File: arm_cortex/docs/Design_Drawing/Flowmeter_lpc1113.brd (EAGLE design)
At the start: 160 x 100 mm, 99 parts, among them IC1 LM7805, IC2 LM324N, IC5 OP07CN, Q4 BSS92, Q5 BSS295, U1 LPC1113FBD48/302,1, U2 LD1117S33CTR, U4 MAX232ACSE+, U5 MAX485CSA+, X1 MKDSN1,5/3-5,08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

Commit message: removed 4-20mA translation circuit. removed the power 10V supply. added +12V and -12V supply regulator. added bridge rectifier
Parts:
- removed C11, C12: 100n, rcl:C0805K
- removed D1, D2: (no value), diode:MINIMELF
- removed D10, D9: 1N4004, diode:DO41-10
- removed D3: (no value), fabisp:NG_SOD123
- removed JP3: (no value), jumper:JP1
- removed PRG_SW1: (no value), SparkFun1:TACTILE_SWITCH_SMD
- removed Q3: (no value), semicon-smd-ipc:SOT23W
- removed Q4: BSS92, transistor-fet:TO92
- removed Q5: BSS295, transistor-fet:TO92
- removed R12: 6k8, rcl:R0805
- removed R13: 10E, rcl:R0805
- removed R20, R22, R24: 10k, resistor:0207/10
- removed R21, R25: 100, rcl:R0805W
- removed R23: 250, resistor:0207/10
- removed R26: 22, rcl:R0805W
- removed SJ8: (no value), jumper:SJ_2
- added RST_SW: (no value), SparkFun1:TACTILE_SWITCH_SMD
- IC1: value LM7805 -> (none); device SparkFun5:78XXL -> v-reg:79XXS
- moved D8 488.0 mm to (143.5, 76.2), turned to 270 degrees
- moved D7 478.1 mm to (137.2, 76.2), turned to 90 degrees
- moved D6 468.9 mm to (132.1, 76.2), turned to 270 degrees
- moved X2 466.9 mm to (137.2, 88.9)
- moved D4 459.8 mm to (127.0, 76.2), turned to 90 degrees
- moved IC3 449.5 mm to (147.3, 66.0)
- moved X3 447.3 mm to (113.0, 6.35)
- moved IC4 437.4 mm to (151.1, 53.3)
- moved C20 381.5 mm to (154.9, 62.2), turned to 90 degrees
- moved JP5 331.2 mm to (96.5, 21.6)
- moved C21 322.6 mm to (90.2, 21.6), turned to 90 degrees
- moved C19 317.9 mm to (66.0, 72.4)
- moved U4 313.2 mm to (66.0, 80.0)
- moved U5 310.1 mm to (83.8, 21.6)
- moved C17 309.6 mm to (58.4, 88.9), turned to 270 degrees
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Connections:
- removed net N$19: D1.C, D2.C, Q3.1
- removed net N$20: C11.2, IC2.7, R21.1
- removed net N$21: Q3.3, R13.2
- removed net N$22: D2.A, D3.CATHODE, R12.2
- removed net N$23: JP3.2, R12.1
- removed net N$25: Q3.2, SJ8.1
- removed net N$40: Q5.1, R21.2
- removed net N$44: C12.1, IC2.9, Q4.2, R23.2
- removed net N$45: C11.1, IC2.10, IC2.6, Q5.3, R20.1, R24.2
- removed net N$46: IC2.5, R22.1
- removed net N$47: C12.2, IC2.8, R25.1
- removed net N$48: Q4.1, R25.2
- removed net N$50: R26.1, X3.2
- removed net N$51: D10.C, D9.A, Q4.3, R26.2
- removed net PWR_SW: SJ8.2
- removed net UC_KA: D1.A, U1.27
- net +12V: no longer D9.C, Q5.2, R23.1, R24.1
- net DAC_VOUT: no longer R22.2
- net GND: now also RST_SW.2; no longer D10.A, D3.ANODE, PRG_SW1.2, R13.1, R20.2, SJ8.3, X3.3
- net N$4: now also RST_SW.4; no longer PRG_SW.4
- net N$5: now also PRG_SW.4; no longer PRG_SW1.4
- net V+: no longer JP3.1

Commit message: removed +12V -12V regulators. added connector for input regulated 12V added lm321 inplace of lm324
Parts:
- removed D4, D6, D7, D8: 1N4004, diode:DO41-10
- removed IC2: LM324N, linear:DIL14
- removed IC4: (no value), v-reg:79XXS
- added C11, C12: 100n, rcl:C0805K
- added D1, D2: 1N4004, diode:DO41-10
- C14: value 100uF/60V -> 100n; device rcl:E5-6 -> rcl:C0805K
- C20: value 1000uF -> 100n; device rcl:C050-035X075@1 -> rcl:C0805K
- C24: value 100n -> 100uF/60V; device rcl:C0805K -> rcl:E5-6
- C25: value 1000uF -> 100n; device rcl:C050-035X075@2 -> rcl:C0805K
- IC3: value (none) -> LM321MF; device v-reg:79XXS -> linear:SOT23-5
- moved X2 558.5 mm to (-158.8, -384.8)
- moved C20 540.0 mm to (-167.6, -370.8), turned to 0 degrees
- moved C14 524.4 mm to (-167.6, -365.8), turned to 0 degrees
- moved IC3 520.4 mm to (-166.4, -349.2)
- moved C24 152.5 mm to (-165.1, -400.1)
- moved C26 97.9 mm to (-165.1, -407.7), turned to 0 degrees
- moved C25 74.7 mm to (-167.6, -375.9)
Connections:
- removed net N$32: IC3.OUT
- removed net N$38: D7.A, D8.C, X2.2
- removed net N$39: D4.A, D6.C, X2.1
- removed net V+: C14.+, D4.C, D8.A, IC3.IN
- removed net V-: C26.+, D6.A, D7.C, IC4.IN
- new net N$19: C24.-, C26.+, X2.2
- new net N$20: D2.C, X2.3
- new net N$21: D1.A, X2.1
- new net N$22: C23.+, C25.1, IC3.5
- net +12V: now also C20.2, C24.+, D1.C; no longer C20.1, C23.+, C24.1, IC2.4
- net -12V: now also C14.1, C26.-, D2.A; no longer C25.1, IC4.OUT
- net 5V: now also C12.2
- net GND: now also C11.1, C12.1, C14.2, C20.1, IC3.2; no longer C14.-, C20.2, C24.2, C26.-, IC2.11, IC3.GND, IC4.GND, X2.3
- net N$15: now also IC3.3; no longer IC2.2
- net N$37: now also IC3.4; no longer IC2.1
- net N$43: now also C11.2
- net SENSOR_SIGNAL: now also IC3.1; no longer IC2.3

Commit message: removed led mosfets
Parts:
- removed IC3: LM321MF, linear:SOT23-5
- removed JP4: (no value), jumper:JP2
- removed JP5: (no value), jumper:JP1
- removed Q1, Q2: (no value), semicon-smd-ipc:SOT23W
- removed SJ6, SJ7: (no value), jumper:SJ
- removed SV1: (no value), con-amp-mt6:MT6-3
- added D3: 1N4004, diode:DO41-10
- added IC2: OP07CN, linear:DIL08
- added X4: MKDSN1,5/3-5,08, con-phoenix-508:MKDSN1,5/3-5,08
- C22: device rcl:C0805K -> rcl:C025-024X044
- D5: device ng:SOD123 -> ng:DO41Z10
- R14, R15, R16, R17, R18: device rcl:R0805W -> rcl:0207/10
- moved D2 541.3 mm to (24.4, 85.1)
- moved D1 525.2 mm to (25.1, 75.2), turned to 180 degrees
- moved C24 524.6 mm to (38.1, 83.6), turned to 180 degrees
- moved C26 524.6 mm to (38.1, 75.9)
- moved C12 508.3 mm to (83.1, 81.5), flipped to the bottom, turned to 90 degrees
- moved C11 493.6 mm to (82.5, 69.8), flipped to the bottom, turned to 270 degrees
- moved C25 486.3 mm to (50.0, 58.9), flipped to the bottom, turned to 90 degrees
- moved X2 473.7 mm to (6.35, 59.2), turned to 90 degrees
- moved C14 462.6 mm to (44.2, 45.5), flipped to the bottom
- moved C20 452.8 mm to (44.5, 29.2), flipped to the bottom, turned to 180 degrees
- moved R19 435.5 mm to (58.2, 41.9)
- moved R11 428.5 mm to (58.2, 37.8)
- moved IC5 414.2 mm to (44.5, 36.8), turned to 90 degrees
- moved R9 402.7 mm to (32.0, 37.6)
- moved R10 402.5 mm to (32.0, 41.1)
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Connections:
- removed net N$11: SJ7.1, SV1.3
- removed net N$12: SJ6.1, SV1.1
- removed net N$19: C24.-, C26.+, X2.2
- removed net N$3: Q2.1, R5.1
- removed net N$35: Q1.1, R4.1
- removed net RXD: SJ6.2
- removed net TXD: SJ7.2
- net +12V: now also D3.C
- net 5V: now also D3.A
- net GND: now also C24.-, C26.+, D5.A, IC2.4, X2.2, X4.2; no longer D5.ANODE, IC3.2, JP4.3, Q1.3, Q2.3, SV1.2
- net LED1: now also U1.21
- net LED2: now also U1.20
- net N$1: now also R4.1; no longer Q1.2
- net N$15: now also IC2.2; no longer IC3.3
- net N$2: now also R5.1; no longer Q2.2
- net N$22: now also IC2.7; no longer IC3.5
- net N$30: now also X4.1; no longer JP4.1
- net N$31: now also X4.3; no longer JP4.2
- net N$33: now also X3.3; no longer X3.1
- net N$34: now also X3.1; no longer JP5.1
- net N$36: now also X3.2; no longer JP5.2
- net N$37: now also IC2.6; no longer IC3.4
- net PULSE: now also D5.C; no longer D5.CATHODE
- net SENSOR_SIGNAL: now also IC2.3; no longer IC3.1

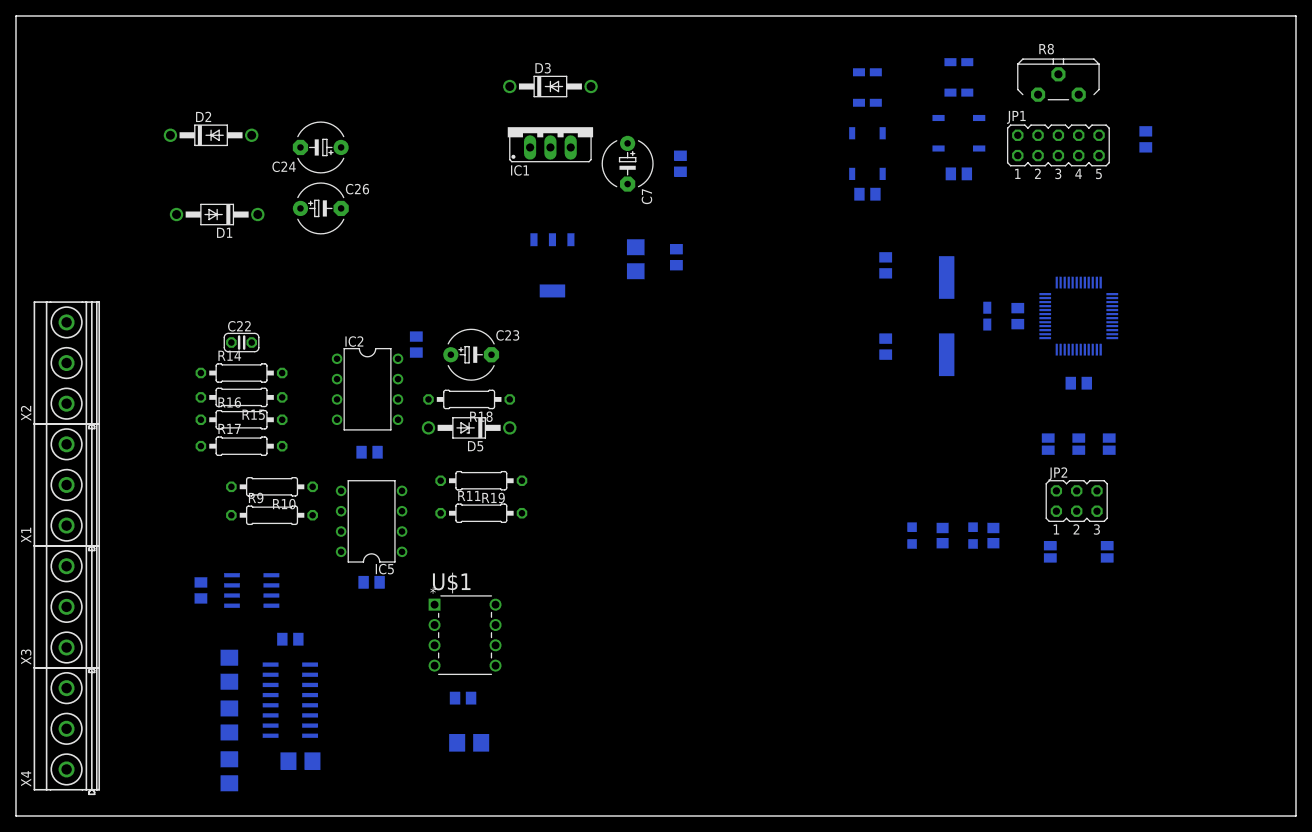
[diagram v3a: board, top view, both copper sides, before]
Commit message: 
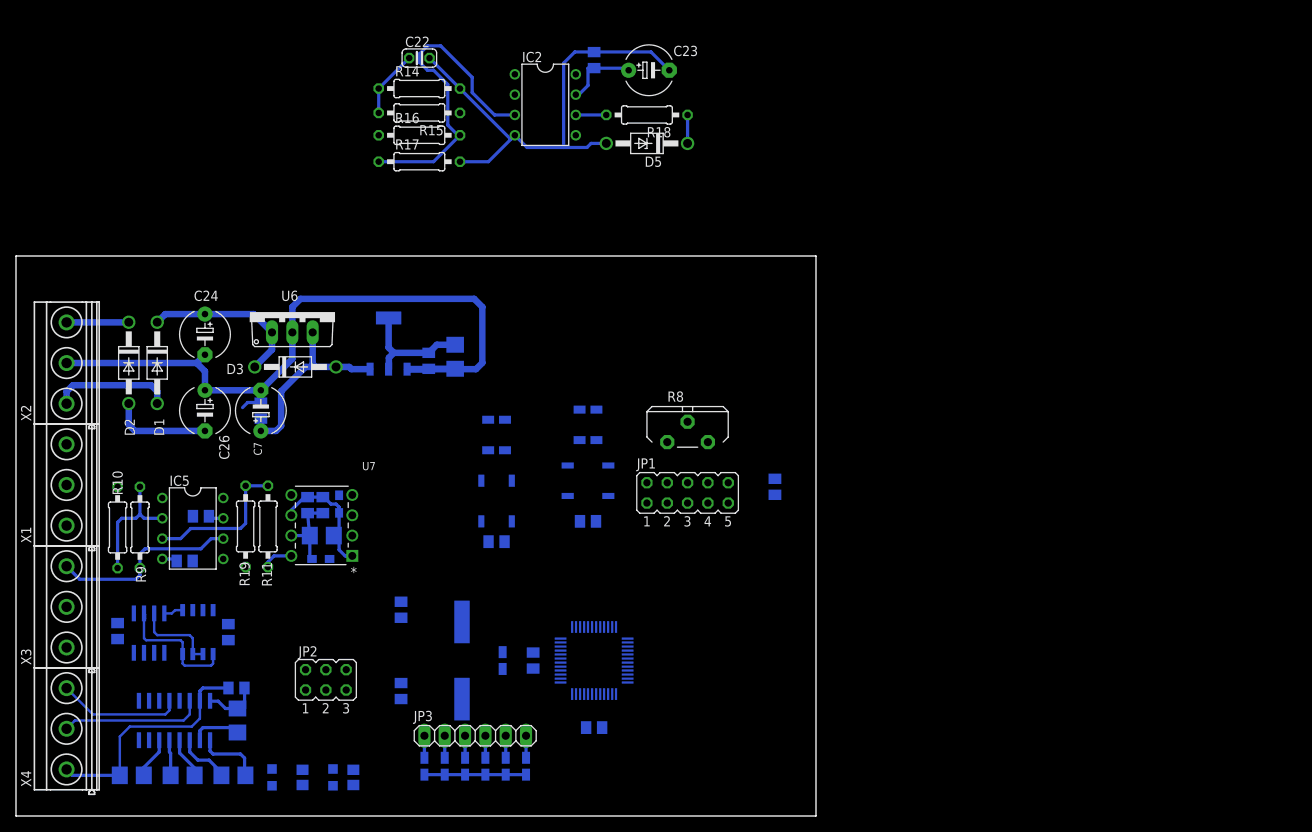
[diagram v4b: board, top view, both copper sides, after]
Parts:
- removed IC1: (no value), v-reg:79XXS
- removed SJ1, SJ2, SJ3, SJ4, SJ5: (no value), jumper:SJ
- removed U$1: MCP4921-E/P, microchip:DIP254P762X432-8
- added C27, C28: 100n, rcl:C0805K
- added JP3: (no value), pinhead:1X06
- added L1, L2: WURTH ELEKTRONIK - 742792095, wuerth-elektronik:0805
- added R12, R13, R20, R21, R22, R23: 10k, rcl:R0805W
- added U6: 7805TV, linear:TO220V
- added U7: MCP4921-E/P, microchip:DIP254P762X432-8
- added U8: SP1490, exar:SO-08
- moved JP2 96.5 mm to (38.7, 17.0)
- moved R5 85.5 mm to (42.2, 4.83)
- moved LED1 85.5 mm to (32.0, 4.83)
- moved LED2 85.5 mm to (39.6, 4.83)
- moved R4 85.5 mm to (35.8, 4.83)
- moved C4 74.3 mm to (72.3, 11.0)
- moved R3 74.3 mm to (60.8, 19.4)
- moved U1 74.3 mm to (72.3, 19.4)
- moved 24MHZ 74.3 mm to (55.8, 19.4)
- moved C1 74.3 mm to (48.1, 15.6)
- moved C2 74.3 mm to (48.1, 25.8)
- moved C5 74.3 mm to (64.6, 19.4)
- moved C3 63.5 mm to (60.1, 34.3)
- moved PRG_SW 63.5 mm to (60.1, 39.4)
- moved R1 63.5 mm to (60.1, 45.7)
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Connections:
- removed net N$10: JP2.1, SJ5.1
- removed net N$18: U$1.7
- removed net N$30: U4.12, X4.1
- removed net N$31: U4.14, X4.3
- removed net N$34: U5.6, X3.1
- removed net N$36: U5.7, X3.2
- removed net N$6: JP2.5, SJ1.1
- removed net N$7: JP2.2, SJ4.2
- removed net N$8: JP2.4, SJ3.2
- removed net N$9: JP2.6, SJ2.2
- new net A: U5.6, U8.5, U8.8, X3.2
- new net B: U5.7, U8.6, U8.7, X3.1
- new net GND1: C10.2, C27.2, C9.-, L1.2, U7.7
- new net N$11: C10.1, C27.1, C9.+, L2.1, U7.1, U7.6
- new net N$12: U4.14, X4.2
- new net SWITCH0: JP3.1, R23.2
- new net SWITCH1: JP3.2, R22.2
- new net SWITCH2: JP3.3, R21.2
- new net SWITCH3: JP3.4, R20.2
- new net SWITCH4: JP3.5, R13.2
- new net SWITCH5: JP3.6, R12.2
- new net UART_RX1: U8.2
- net +12V: now also U6.1; no longer IC1.IN
- net /RESET: now also JP2.5; no longer SJ1.2
- net 5V: now also C16.-, C19.2, C21.2, C28.2, L2.2, U4.16, U5.8, U6.3, U8.1; no longer IC1.OUT
- net DAC_VOUT: now also U7.8; no longer U$1.8
- net GND: now also C28.1, JP2.1, L1.1, U4.15, U6.2, U8.4, X4.1; no longer C10.2, C9.-, IC1.GND, SJ5.2, X4.2
- net LCD_EN: now also U1.43; no longer U1.9
- net LCD_R/W: now also U1.37; no longer U1.17
- net LCD_RS: now also U1.36; no longer U1.30
- net LDAC: now also U1.48, U7.5; no longer U$1.5, U1.37
- net N$13: now also U4.12, X4.3; no longer U$1.6
- net SPI1_CS: now also U7.2; no longer U$1.2
- net SPI1_MOSI: now also U7.4; no longer U$1.4
- net SPI1_SCK: now also U7.3; no longer U$1.3
- net SWDCLK: now also JP2.6; no longer SJ2.1
- net SWDIO: now also JP2.4; no longer SJ3.1
- net UART_TX: now also U8.3
- net VCC: now also JP2.2, R12.1, R13.1, R20.1, R21.1, R22.1, R23.1; no longer C10.1, C16.-, C19.2, C21.2, C9.+, SJ4.1, U$1.1, U4.16, U5.8
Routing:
- net GND: track 0.00 -> 182.5 mm
- net SENSOR_SIGNAL: track 0.00 -> 41.4 mm
- net 5V: track 0.00 -> 35.7 mm
- net N$33: track 0.00 -> 23.9 mm
- net +12V: track 0.00 -> 22.8 mm
- net N$17: track 0.00 -> 18.7 mm
- net N$12: track 0.00 -> 17.8 mm
- net N$11: track 0.00 -> 16.2 mm
- net A: track 0.00 -> 16.1 mm
- net N$16: track 0.00 -> 15.7 mm
- net N$13: track 0.00 -> 15.6 mm
- net N$43: track 0.00 -> 15.0 mm
- net N$21: track 0.00 -> 15.0 mm
- net -12V: track 0.00 -> 14.4 mm
- net VCC: track 0.00 -> 12.7 mm
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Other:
- board size 160 x 100 mm -> 100 x 70 mm

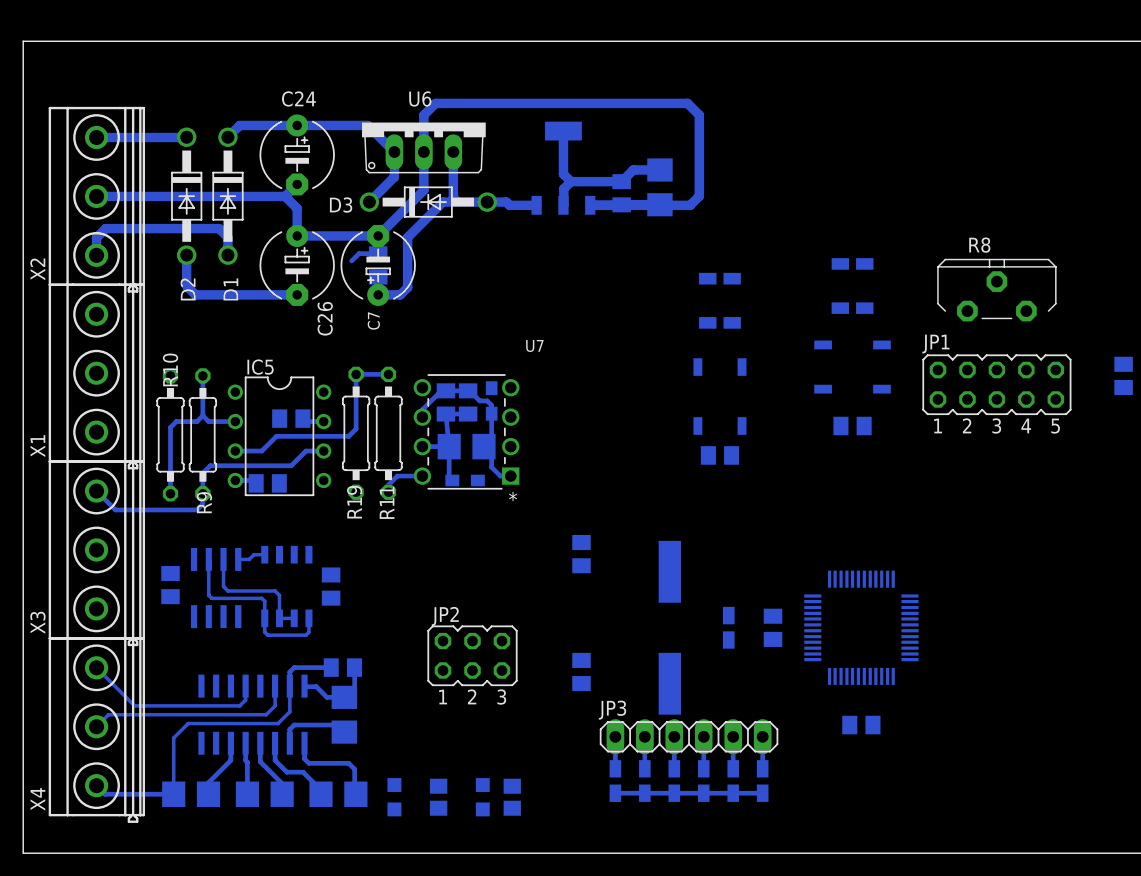
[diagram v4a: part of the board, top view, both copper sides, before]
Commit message: 
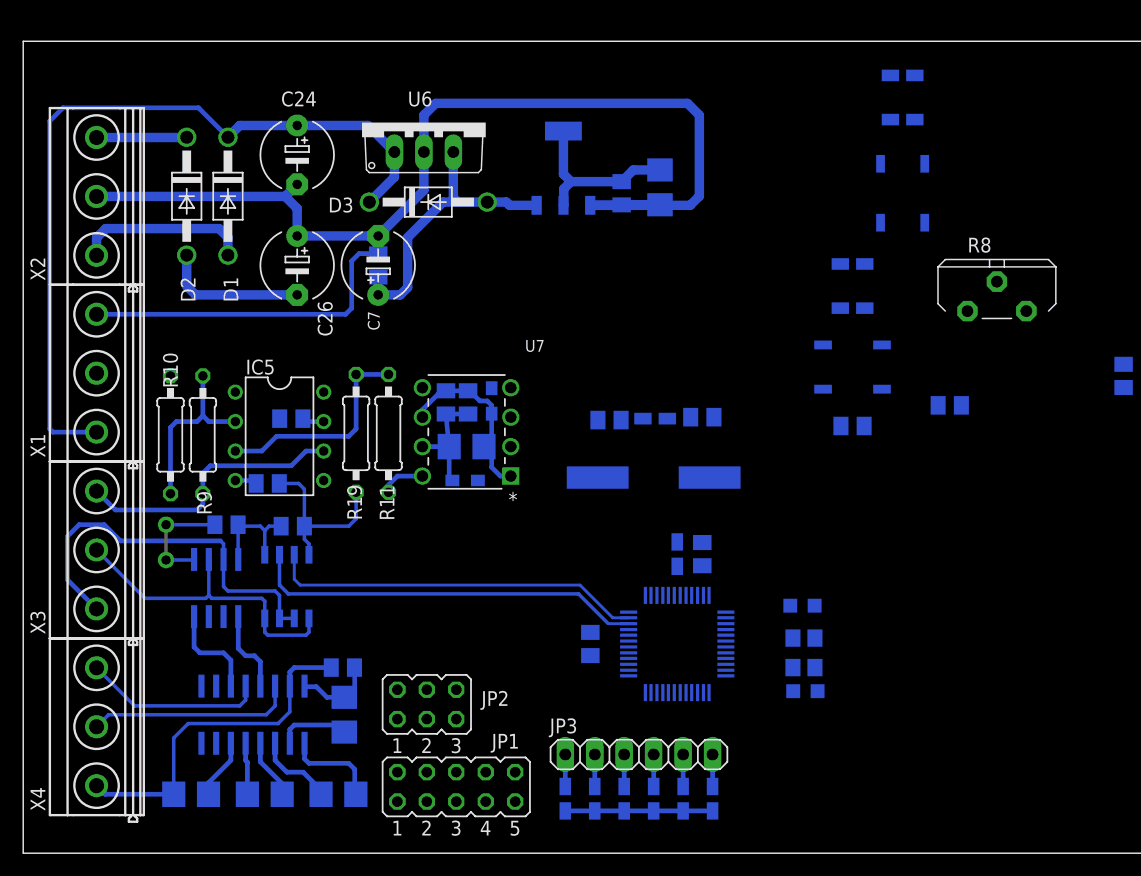
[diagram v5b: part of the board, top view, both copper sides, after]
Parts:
- added R24: 50E, rcl:R0805W
- moved JP1 58.1 mm to (37.3, 5.71)
- moved LED1 36.6 mm to (67.4, 14.0), turned to 90 degrees
- moved R4 33.4 mm to (67.3, 16.0), turned to 0 degrees
- moved LED2 32.1 mm to (67.2, 21.3), turned to 90 degrees
- moved R5 28.6 mm to (67.3, 18.5), turned to 0 degrees
- moved C4 24.4 mm to (48.9, 18.0), turned to 270 degrees
- moved PRG_SW 23.6 mm to (75.8, 56.9)
- moved R1 23.6 mm to (75.8, 63.2)
- moved R2 23.6 mm to (75.8, 67.1)
- moved C1 21.9 mm to (50.5, 37.3), turned to 0 degrees
- moved C3 20.3 mm to (79.9, 38.6)
- moved R3 19.1 mm to (54.5, 37.5), turned to 180 degrees
- moved U1 15.9 mm to (56.4, 18.0), turned to 270 degrees
- moved C2 15.7 mm to (58.5, 37.6), turned to 0 degrees
- moved 24MHZ 13.0 mm to (54.4, 32.4), turned to 180 degrees
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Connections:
- removed net UART_RX1: U8.2
- new net N$6: 24MHZ.2, C2.2, R24.2, R3.2
- net UART_RX: now also U8.2
- net XTAL_OUT: now also R24.1; no longer 24MHZ.2, C2.2, R3.2
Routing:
- net GND: track 182.5 -> 233.7 mm, vias 0 -> 2
- net +12V: track 22.8 -> 70.4 mm
- net UART_RX: track 0.00 -> 41.3 mm
- net UART_TX: track 0.30 -> 41.1 mm
- net B: track 10.7 -> 33.9 mm
- net A: track 16.1 -> 28.4 mm
- net 5V: track 35.7 -> 42.2 mm
